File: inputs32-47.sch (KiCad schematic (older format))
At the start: 160 parts

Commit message: updated labels for schematics 32-47 and 48-63
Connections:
- net labels added: in39_v, in40_v, in41_v, in42_v, in43_v, in44_v, in45_v, in46_v, in47_v
- net labels removed: in10_v, in11_v, in12_v, in13_v, in14_v, in15_v, in7_v, in8_v, in9_v
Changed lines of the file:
@@
 in38_v
 Text HLabel 2000 3300 0    60   Input ~ 0
-in7_v
+in39_v
 Text HLabel 2000 3600 0    60   Input ~ 0
-in8_v
+in40_v
 Text HLabel 2000 3900 0    60   Input ~ 0
-in9_v
+in41_v
 Text HLabel 2000 4200 0    60   Input ~ 0
-in10_v
+in42_v
 Text HLabel 2000 4500 0    60   Input ~ 0
-in11_v
+in43_v
 Text HLabel 2000 4800 0    60   Input ~ 0
-in12_v
+in44_v
 Text HLabel 2000 5100 0    60   Input ~ 0
-in13_v
+in45_v
 Text HLabel 2000 5400 0    60   Input ~ 0
-in14_v
+in46_v
 Text HLabel 2000 5700 0    60   Input ~ 0
-in15_v
+in47_v
 Text HLabel 2850 6000 3    60   Input ~ 0
 out0_i

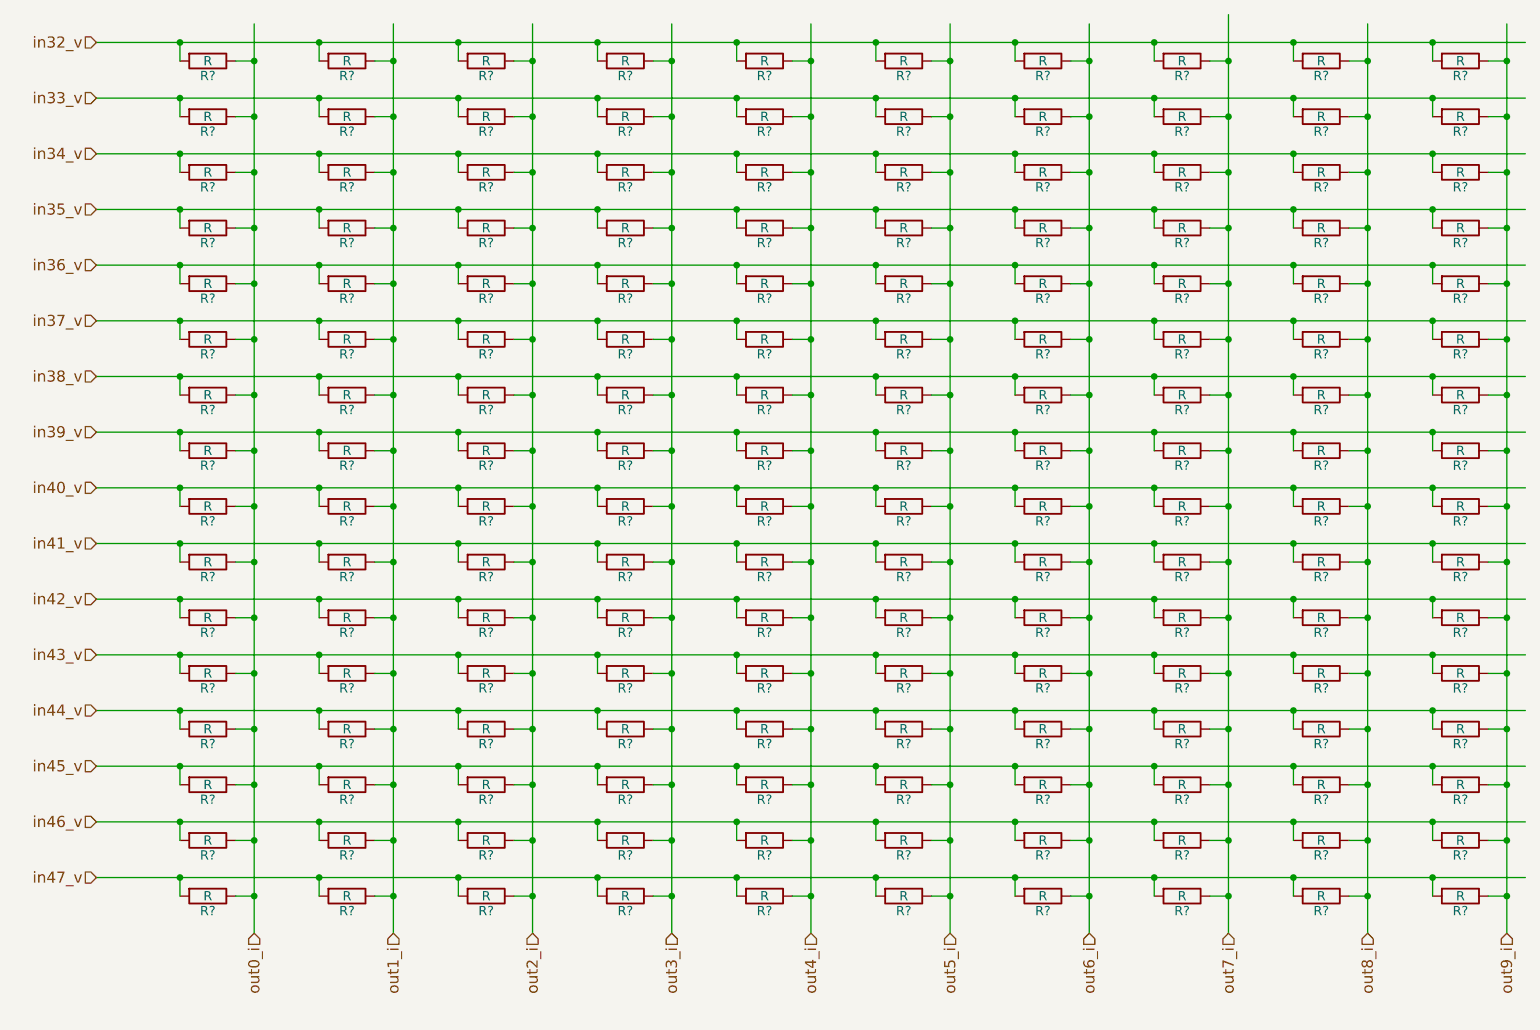
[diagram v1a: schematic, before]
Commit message: Updated resistors 32-63
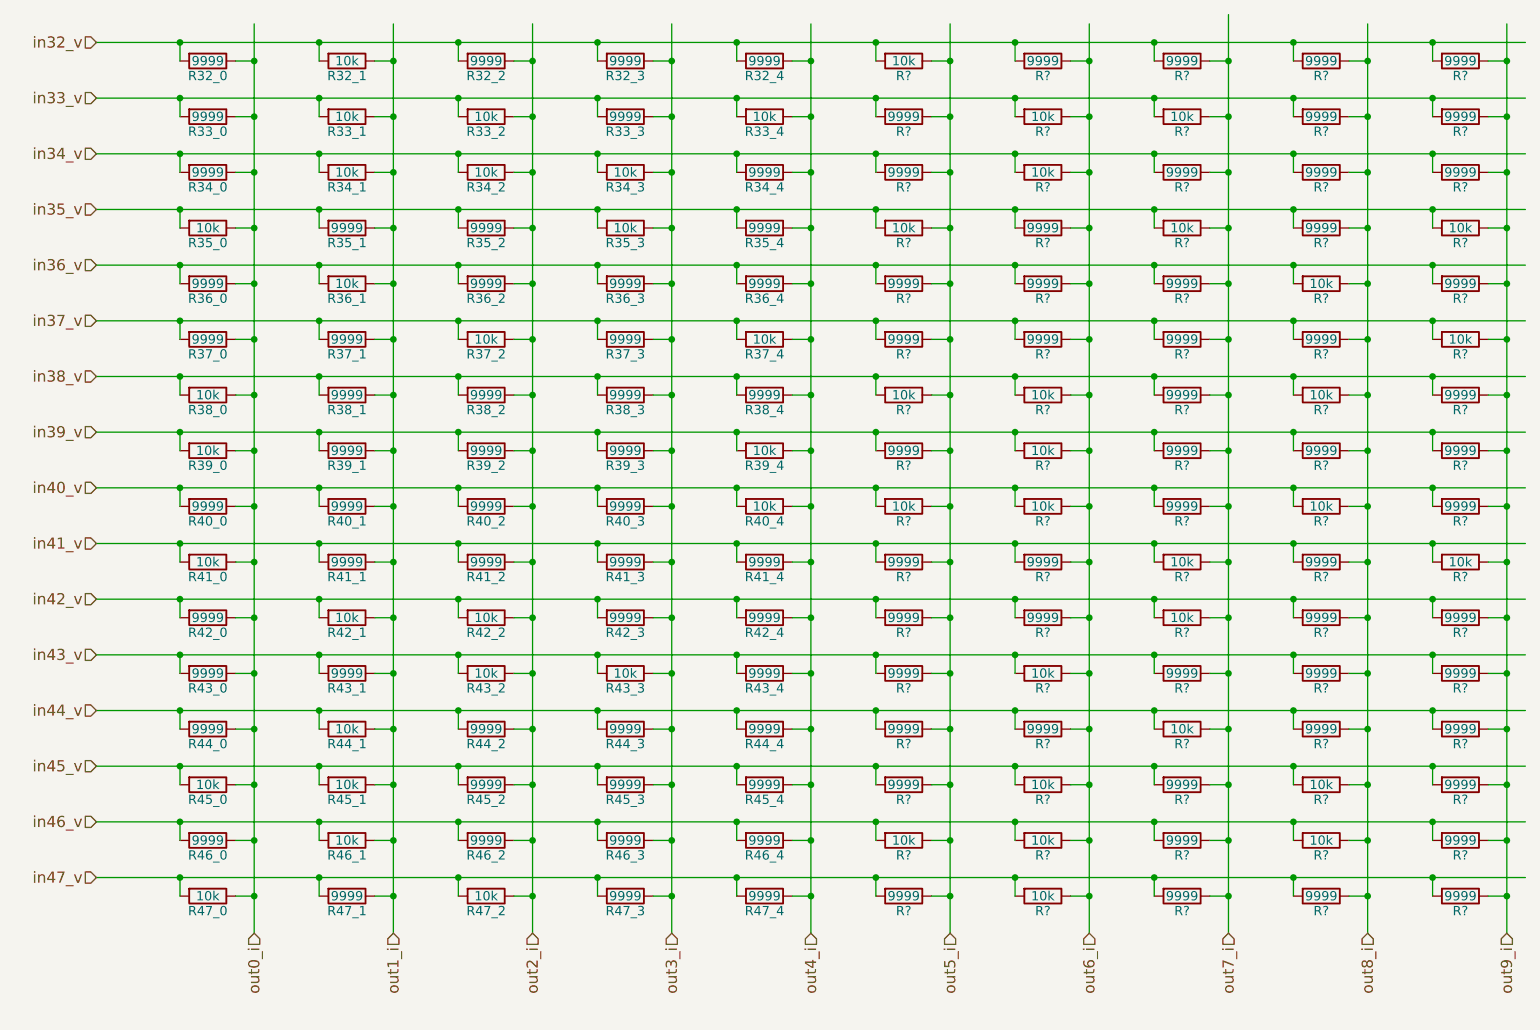
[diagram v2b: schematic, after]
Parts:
- R32_0, R32_2, R32_3, R32_4, R33_0, R33_3, R34_0, R34_4, R35_1, R35_2, R35_4, R36_0, R36_2, R36_3, R36_4, R37_0, R37_1, R37_3, R38_1, R38_2, R38_3, R38_4, R39_1, R39_2, R39_3, R40_0, R40_1, R40_2, R40_3, R41_1, R41_2, R41_3, R41_4, R42_0, R42_3, R42_4, R43_0, R43_1, R43_4, R44_0, R44_2, R44_3, R44_4, R45_2, R45_3, R45_4, R46_0, R46_2, R46_3, R46_4, R47_1, R47_3, R47_4: renamed from R?; value R -> 9999
- R32_1, R33_1, R33_2, R33_4, R34_1, R34_2, R34_3, R35_0, R35_3, R36_1, R37_2, R37_4, R38_0, R39_0, R39_4, R40_4, R41_0, R42_1, R42_2, R43_2, R43_3, R44_1, R45_0, R45_1, R46_1, R47_0, R47_2: renamed from R?; value R -> 10k
- R? (x27): value R -> 10k
- R? (x53): value R -> 9999

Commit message: Finished Resistors 32-47
Still need to finish naming 48-63
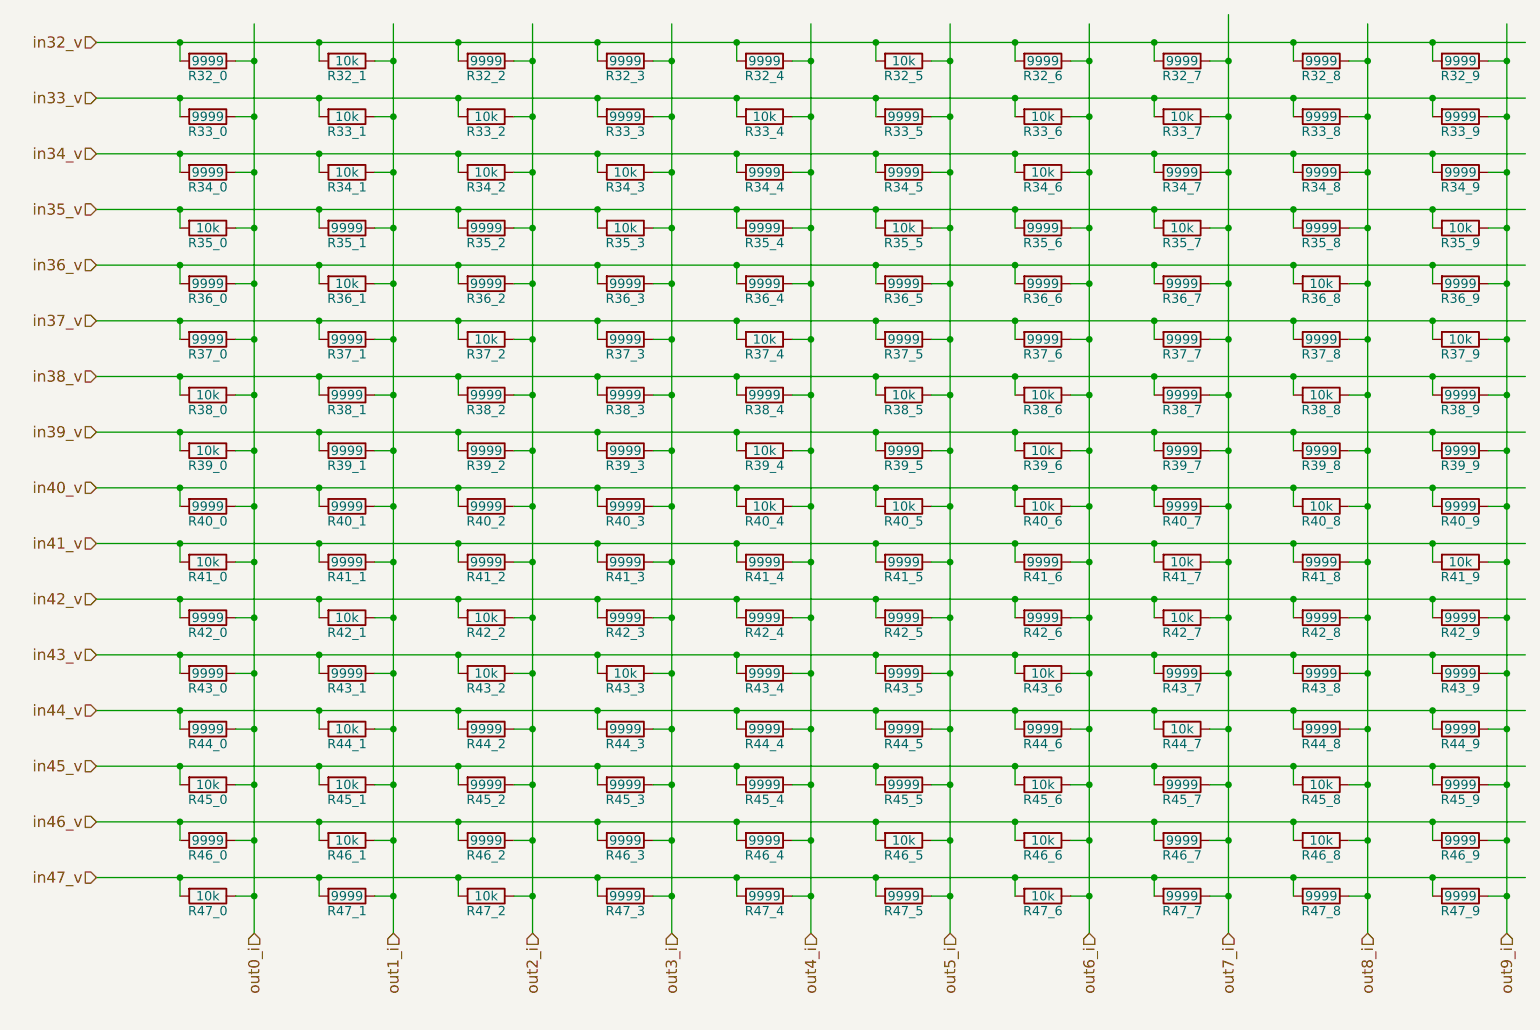
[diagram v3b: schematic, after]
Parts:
- gave numbers to parts that had none: 80

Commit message: Added footprints, finished schematic, began PCB layout
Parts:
- R32_0, R32_1, R32_2, R32_3, R32_4, R32_5, R32_6, R32_7, R32_8, R32_9, R33_0, R33_1, R33_2, R33_3, R33_4, R33_5, R33_6, R33_7, R33_8, R33_9, R34_0, R34_1, R34_2, R34_3, R34_4, R34_5, R34_6, R34_7, R34_8, R34_9, R35_0, R35_1, R35_2, R35_3, R35_4, R35_5, R35_6, R35_7, R35_8, R35_9, R36_0, R36_1, R36_2, R36_3, R36_4, R36_5, R36_6, R36_7, R36_8, R36_9, R37_0, R37_1, R37_2, R37_3, R37_4, R37_5, R37_6, R37_7, R37_8, R37_9, R38_0, R38_1, R38_2, R38_3, R38_4, R38_5, R38_6, R38_7, R38_8, R38_9, R39_0, R39_1, R39_2, R39_3, R39_4, R39_5, R39_6, R39_7, R39_8, R39_9, R40_0, R40_1, R40_2, R40_3, R40_4, R40_5, R40_6, R40_7, R40_8, R40_9, R41_0, R41_1, R41_2, R41_3, R41_4, R41_5, R41_6, R41_7, R41_8, R41_9, R42_0, R42_1, R42_2, R42_3, R42_4, R42_5, R42_6, R42_7, R42_8, R42_9, R43_0, R43_1, R43_2, R43_3, R43_4, R43_5, R43_6, R43_7, R43_8, R43_9, R44_0, R44_1, R44_2, R44_3, R44_4, R44_5, R44_6, R44_7, R44_8, R44_9, R45_0, R45_1, R45_2, R45_3, R45_4, R45_5, R45_6, R45_7, R45_8, R45_9, R46_0, R46_1, R46_2, R46_3, R46_4, R46_5, R46_6, R46_7, R46_8, R46_9, R47_0, R47_1, R47_2, R47_3, R47_4, R47_5, R47_6, R47_7, R47_8, R47_9: footprint (none) -> Resistors_SMD:R_1206

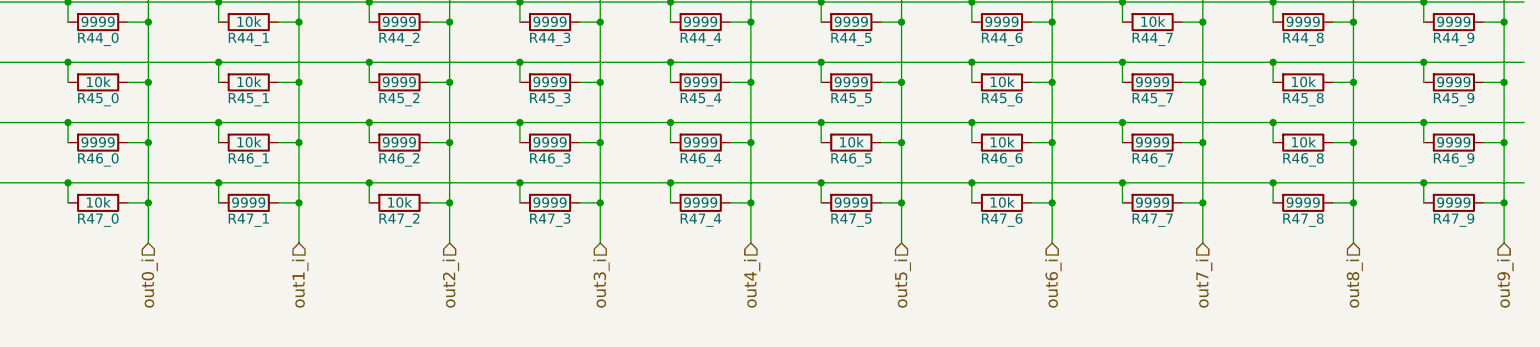
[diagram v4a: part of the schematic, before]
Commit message: fixed resistor schematic errors
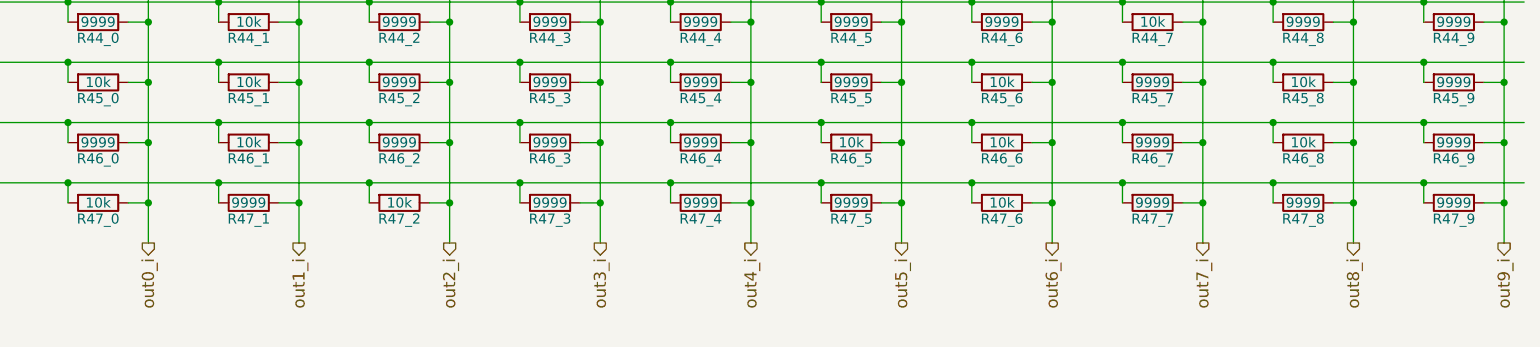
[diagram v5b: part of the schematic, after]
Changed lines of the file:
@@
 $Descr A4 11693 8268
 encoding utf-8
-Sheet 6 7
+Sheet 5 7
 Title ""
 Date ""
@@
 Text HLabel 2000 5700 0    60   Input ~ 0
 in47_v
-Text HLabel 2850 6000 3    60   Input ~ 0
+Text HLabel 2850 6000 3    60   Output ~ 0
 out0_i
-Text HLabel 3600 6000 3    60   Input ~ 0
+Text HLabel 3600 6000 3    60   Output ~ 0
 out1_i
-Text HLabel 4350 6000 3    60   Input ~ 0
+Text HLabel 4350 6000 3    60   Output ~ 0
 out2_i
-Text HLabel 5100 6000 3    60   Input ~ 0
+Text HLabel 5100 6000 3    60   Output ~ 0
 out3_i
-Text HLabel 5850 6000 3    60   Input ~ 0
+Text HLabel 5850 6000 3    60   Output ~ 0
 out4_i
-Text HLabel 6600 6000 3    60   Input ~ 0
+Text HLabel 6600 6000 3    60   Output ~ 0
 out5_i
-Text HLabel 7350 6000 3    60   Input ~ 0
+Text HLabel 7350 6000 3    60   Output ~ 0
 out6_i
-Text HLabel 8100 6000 3    60   Input ~ 0
+Text HLabel 8100 6000 3    60   Output ~ 0
 out7_i
-Text HLabel 8850 6000 3    60   Input ~ 0
+Text HLabel 8850 6000 3    60   Output ~ 0
 out8_i
-Text HLabel 9600 6000 3    60   Input ~ 0
+Text HLabel 9600 6000 3    60   Output ~ 0
 out9_i
 $Comp
